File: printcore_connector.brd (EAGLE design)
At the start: 80 x 10 mm, 3 parts

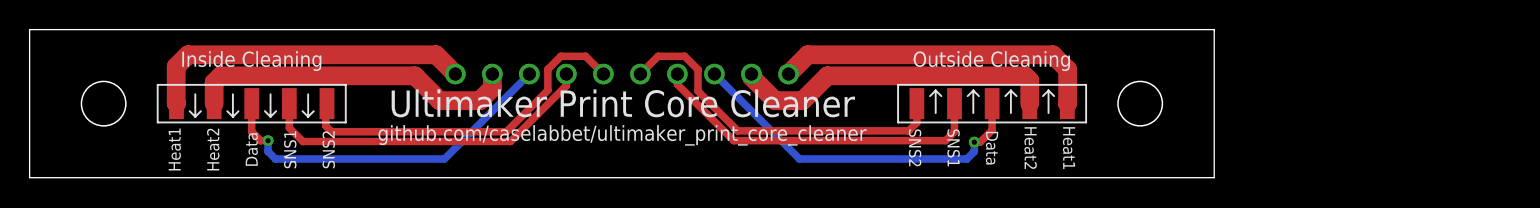
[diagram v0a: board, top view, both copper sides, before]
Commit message: Silcscreen and 3D packages update
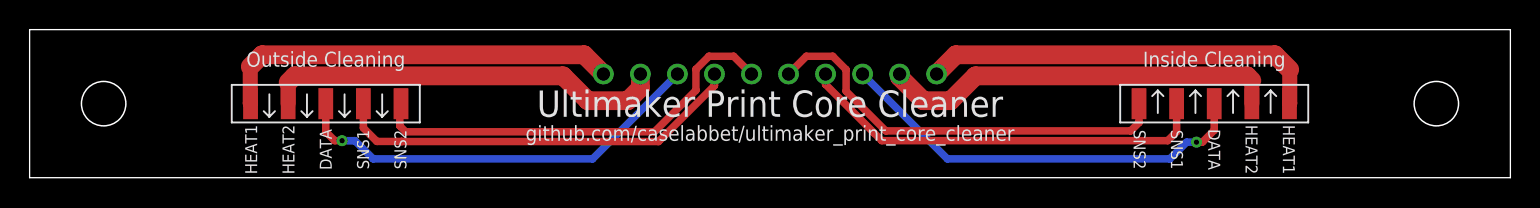
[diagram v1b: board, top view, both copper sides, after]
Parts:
- moved U$3 15.0 mm to (80.0, 5.00)
- moved CONNECTOR 10.0 mm to (50.0, 7.00)
- moved U$1 5.00 mm to (20.0, 5.00)
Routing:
- net PT100_2_R: track 23.6 -> 28.6 mm
- net PT100_2_L: track 23.9 -> 28.9 mm
- net PT100_1_L: track 23.1 -> 28.1 mm
- net HEATER_2_R: track 22.0 -> 27.0 mm
- net HEATER_1_R: track 22.1 -> 27.1 mm
- net HEATER_1_L: track 22.2 -> 27.2 mm
- net PT100_1_R: track 23.1 -> 28.1 mm
- net HEATER_2_L: track 22.4 -> 27.4 mm
- net DATA_R: track 24.1 -> 28.7 mm
- net DATA_L: track 24.2 -> 28.8 mm
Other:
- board size 80 x 10 mm -> 100 x 10 mm
- board text added: "Created by: Isak Åslund Autumn 2019 | Sweden"
- board text added: "HEAT1 HEAT2 DATA SNS1 SNS2"
- board text removed: "Heat1 Heat2 Data SNS1 SNS2"
